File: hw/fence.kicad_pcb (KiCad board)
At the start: 2 copper layers, 52.1 x 73.7 mm, 9 parts, among them J1 Conn_01x02_Male, J2 Conn_01x08_Female, J3 Conn_01x02_Male, J4 Conn_01x08_Female, J5 Conn_01x04_Male, U1 4N25, U2 4N25

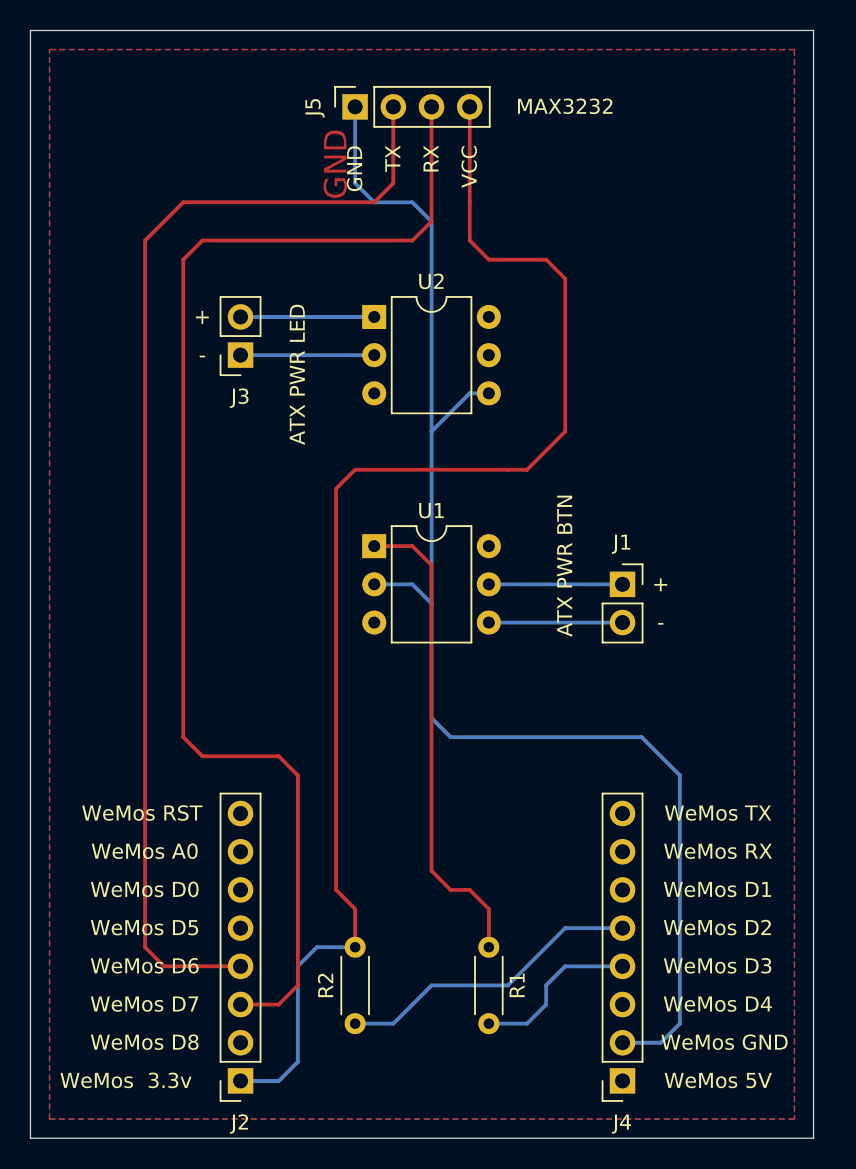
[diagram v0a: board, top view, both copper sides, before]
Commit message: fix HW: wemos header distance
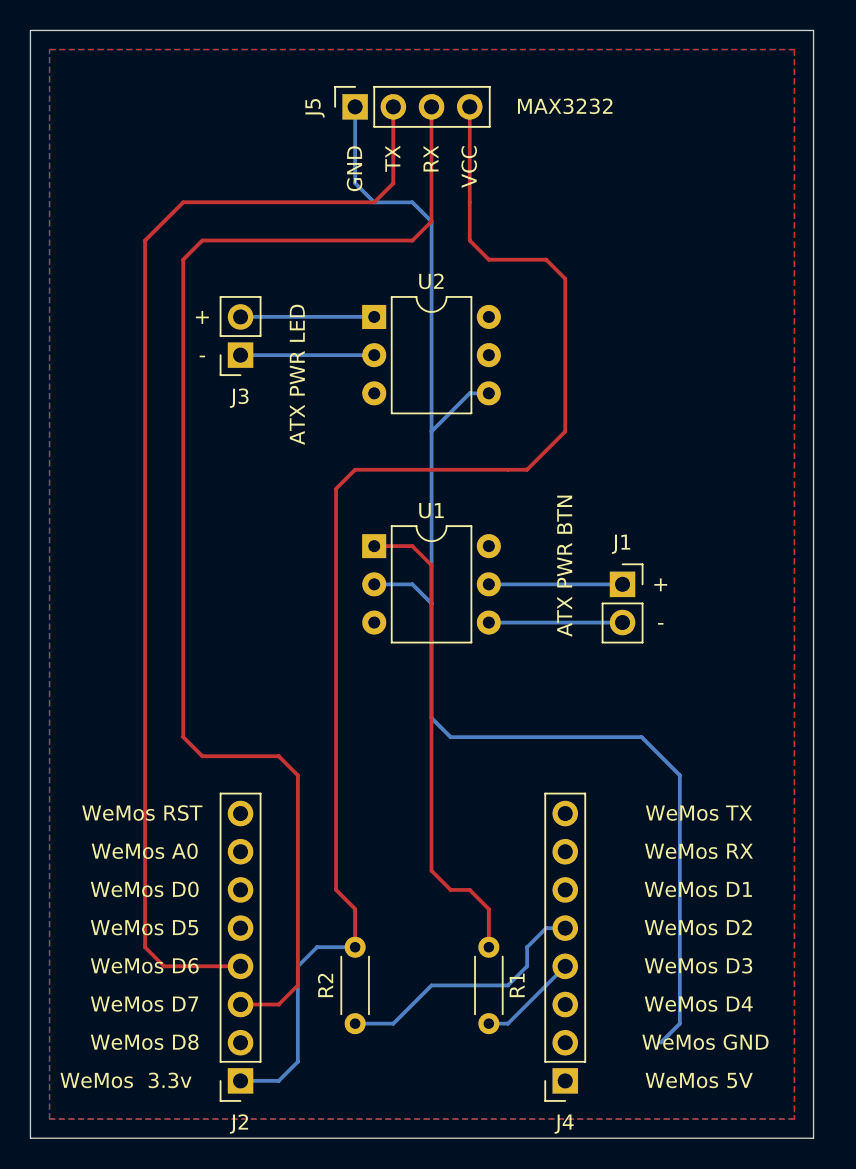
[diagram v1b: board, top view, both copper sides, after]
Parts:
- moved J4 3.81 mm to (61.0, 110.5)
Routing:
- net Net-(J4-Pad4): track 11.2 -> 6.66 mm
- net Net-(J4-Pad5): track 20.4 -> 17.3 mm
- net Net-(J4-Pad2): track 92.4 -> 89.8 mm

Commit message: Fix: WeMos pin5 leftover
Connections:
- U2 pad 5: Net-(U2-Pad5) -> Net-(J2-Pad5)
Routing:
- net Net-(J2-Pad5): track 0.00 -> 47.2 mm
- net Net-(J4-Pad2): track 89.8 -> 93.9 mm

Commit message: PCB and hompage updated
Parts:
- moved J5 2.54 mm to (47.0, 48.3)
- moved J2 1.27 mm to (40.6, 110.5)
- moved R1 1.27 mm to (54.6, 101.6)
- moved J4 1.27 mm to (62.2, 110.5)
- moved R2 1.27 mm to (48.3, 106.7)
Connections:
- U2 pad 5: Net-(J2-Pad5) -> Net-(J4-Pad5)
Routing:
- net Net-(J4-Pad2): track 93.9 -> 192.9 mm
- net Net-(J2-Pad5): track 47.2 -> 0.00 mm
- net Net-(J4-Pad5): track 17.3 -> 59.9 mm
- net Net-(R1-Pad1): track 32.1 -> 42.3 mm
- net Net-(J2-Pad1): track 89.3 -> 99.2 mm
- net Net-(J2-Pad3): track 83.9 -> 89.5 mm
- net Net-(J2-Pad4): track 77.0 -> 81.6 mm
- net Net-(J4-Pad4): track 6.66 -> 9.20 mm
- removed copper zone on F.Cu, net Net-(J4-Pad2)
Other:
- board text removed: "-"
- board text removed: "Fence v0.2"
- board text removed: "GND"
- board text removed: "MAX3232"
- board text removed: "RX"
- board text removed: "TX"
- board text removed: "VCC"
- board text removed: "WeMos 3.3v"
- board text removed: "WeMos 5V"
- board text removed: "WeMos A0"
- board text removed: "WeMos D0"
- board text removed: "WeMos D1"
- board text removed: "WeMos D2"
- board text removed: "WeMos D3"
- board text removed: "WeMos D4"
- board text removed: "WeMos D5"
- board text removed: "WeMos D6"
- board text removed: "WeMos D7"
- board text removed: "WeMos D8"
- board text removed: "WeMos GND"
- board text removed: "WeMos RST"
- board text removed: "WeMos RX"
- board text removed: "WeMos TX"

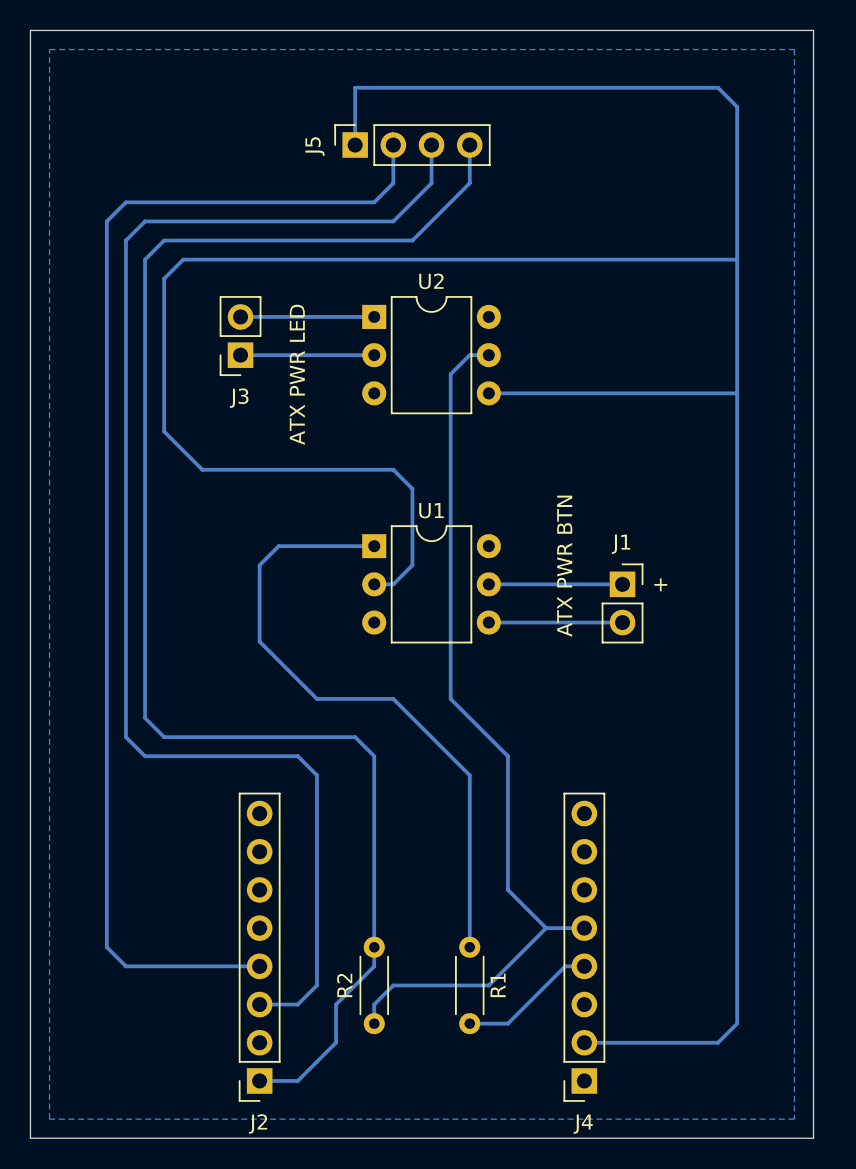
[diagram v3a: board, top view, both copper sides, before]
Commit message: Bundle update
* pcb refactor & fixes
* schetch minor cosmethics
* html buttons rename and synchronization with indicators
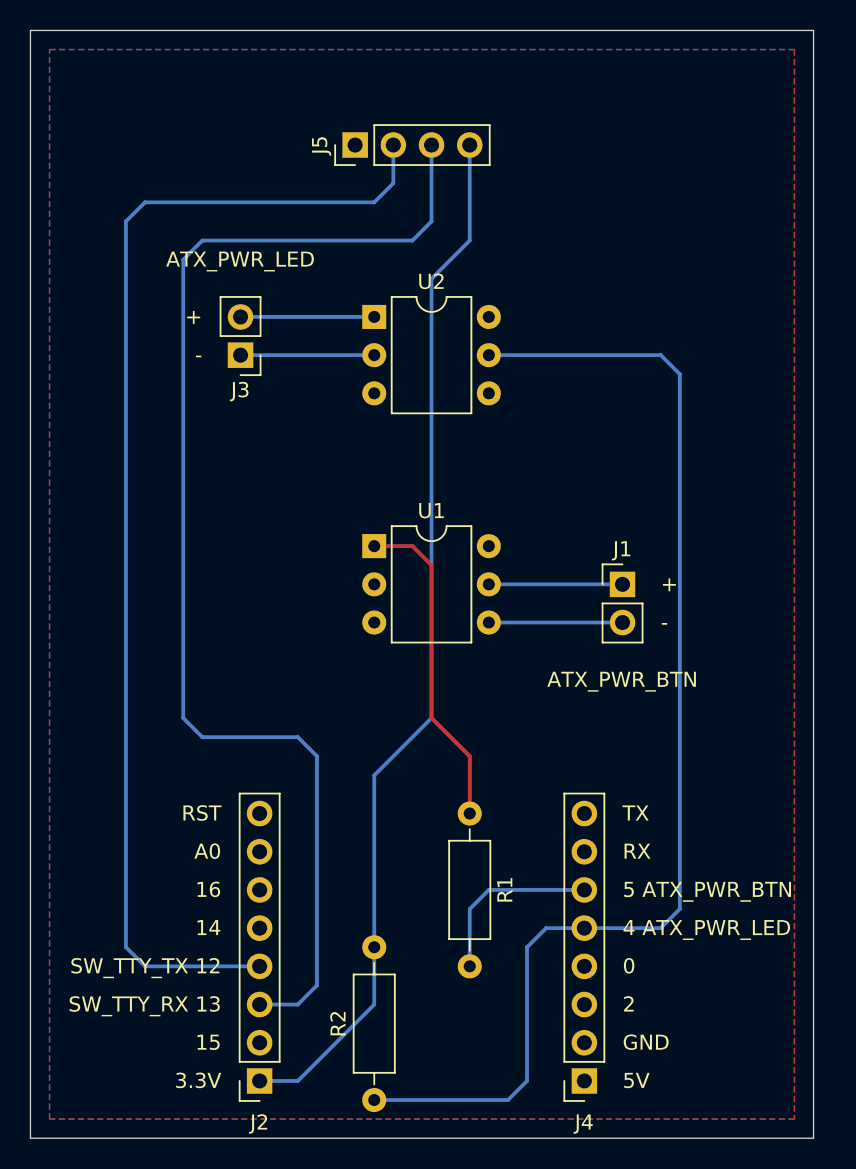
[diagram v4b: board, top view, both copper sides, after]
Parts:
- J1, J3: footprint Connector_PinSocket_2.54mm:PinSocket_1x02_P2.54mm_Vertical -> Connector_PinHeader_2.54mm:PinHeader_1x02_P2.54mm_Vertical
- J5: footprint Connector_PinSocket_2.54mm:PinSocket_1x04_P2.54mm_Vertical -> Connector_PinHeader_2.54mm:PinHeader_1x04_P2.54mm_Vertical
- R1: value R_US -> 220; footprint Resistor_THT:R_Axial_DIN0204_L3.6mm_D1.6mm_P5.08mm_Horizontal -> Resistor_THT:R_Axial_DIN0207_L6.3mm_D2.5mm_P10.16mm_Horizontal
- R2: value R_US -> 10k; footprint Resistor_THT:R_Axial_DIN0204_L3.6mm_D1.6mm_P5.08mm_Horizontal -> Resistor_THT:R_Axial_DIN0207_L6.3mm_D2.5mm_P10.16mm_Horizontal
- moved R1 8.89 mm to (54.6, 92.7)
- moved R2 5.08 mm to (48.3, 111.8)
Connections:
- R1 pad 2: Net-(J4-Pad4) -> Net-(J4-Pad6)
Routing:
- net Net-(J4-Pad2): track 192.9 -> 0.00 mm
- net Net-(J2-Pad1): track 99.2 -> 69.5 mm
- net Net-(R1-Pad1): track 42.3 -> 21.9 mm
- net Net-(J4-Pad5): track 59.9 -> 79.6 mm
- net Net-(J4-Pad6): track 0.00 -> 12.0 mm
- net Net-(J4-Pad4): track 9.20 -> 0.00 mm
- net Net-(J2-Pad3): track 89.5 -> 82.6 mm
- net Net-(J2-Pad4): track 81.6 -> 79.0 mm
- added copper zone on F.Cu, net Net-(J4-Pad2)
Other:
- board text added: "-"
- board text added: "0"
- board text added: "14"
- board text added: "15"
- board text added: "16"
- board text added: "2"
- board text added: "3.3V"
- board text added: "4 ATX_PWR_LED"
- board text added: "5 ATX_PWR_BTN"
- board text added: "5V"
- board text added: "A0"
- board text added: "ATX_PWR_BTN"
- board text added: "ATX_PWR_LED"
- board text added: "GND"
- board text added: "RST"
- board text added: "RX"
- board text added: "SW_TTY_RX 13"
- board text added: "SW_TTY_TX 12"
- board text added: "TX"
- board text removed: "ATX PWR BTN"
- board text removed: "ATX PWR LED"
